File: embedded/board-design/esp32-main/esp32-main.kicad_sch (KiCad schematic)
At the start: 3 parts, among them J1 Conn_ARM_JTAG_SWD_10, U1 ESP32-WROVER-E, U2 BD48ExxG

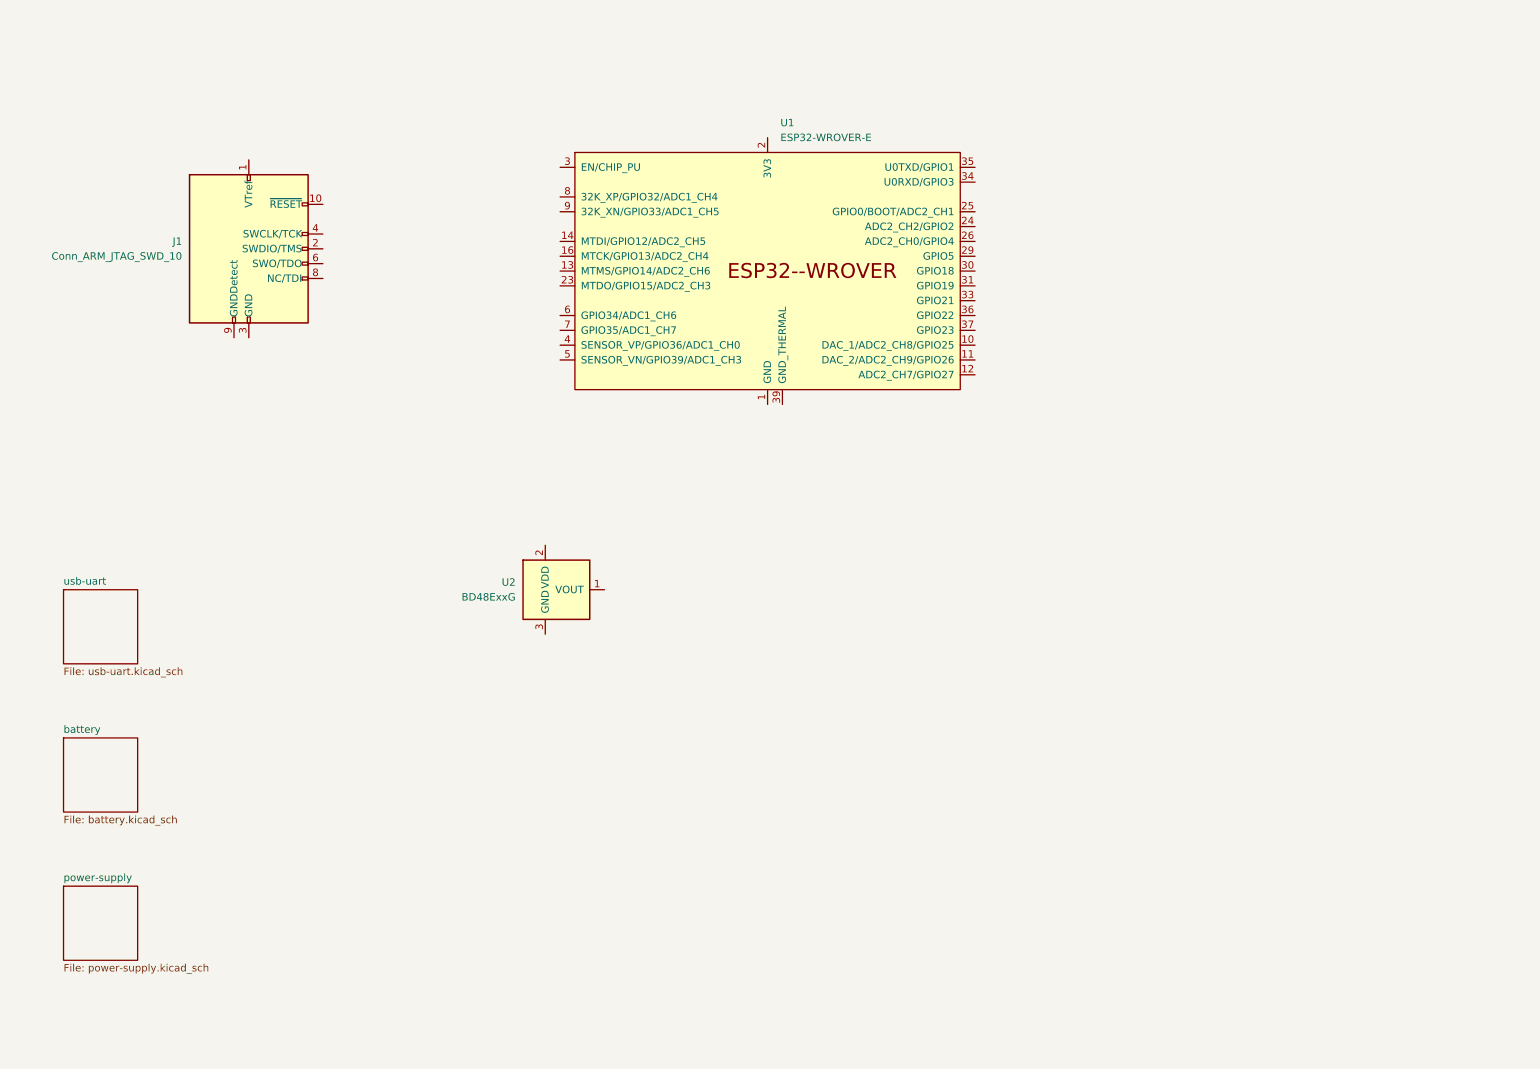
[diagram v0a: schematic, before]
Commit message: [bike-embedded-app]
Finished first schematic draft.

Signed-off-by: Nicolae-Andrei Vasile <vasilenicolaeandrei@gmail.com>
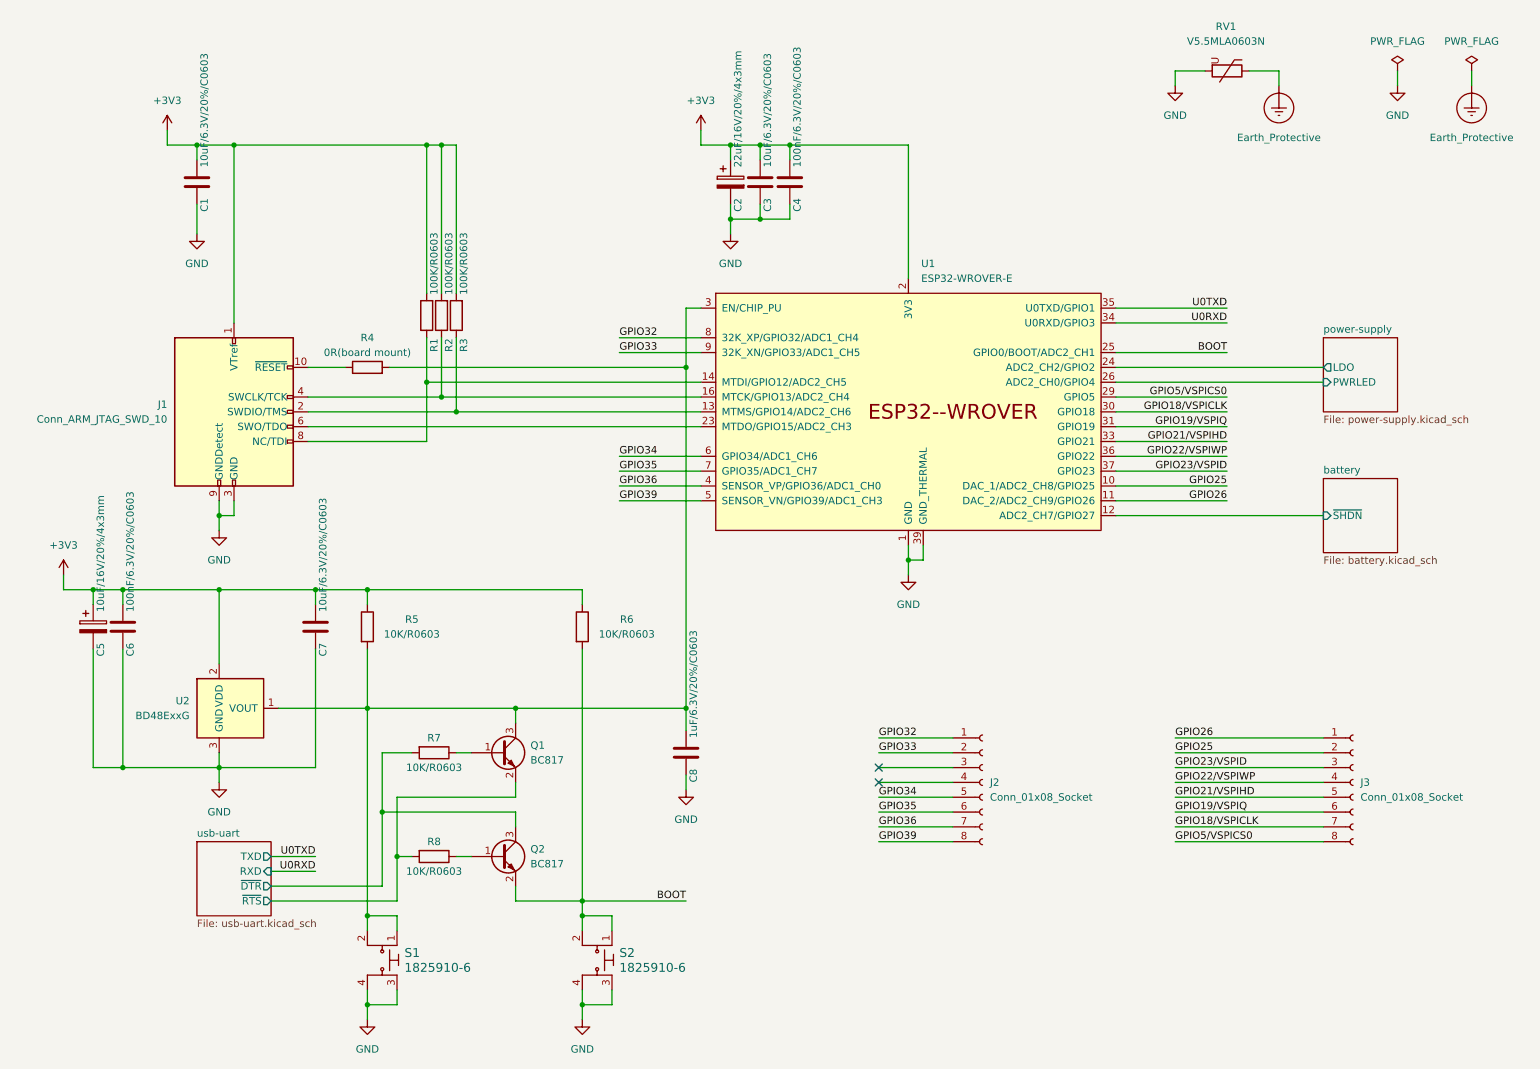
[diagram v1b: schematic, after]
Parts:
- added C1, C3, C7: 10uF/6.3V/20%/C0603, Capacitor_SMD:C_0603_1608Metric_Pad1.08x0.95mm_HandSolder, symbol Device:C
- added C2: 22uF/16V/20%/4x3mm, Capacitor_SMD:CP_Elec_4x3, symbol Device:C_Polarized
- added C4, C6: 100nF/6.3V/20%/C0603, Capacitor_SMD:C_0603_1608Metric_Pad1.08x0.95mm_HandSolder, symbol Device:C
- added C5: 10uF/16V/20%/4x3mm, Capacitor_SMD:CP_Elec_4x3, symbol Device:C_Polarized
- added C8: 1uF/6.3V/20%/C0603, Capacitor_SMD:C_0603_1608Metric_Pad1.08x0.95mm_HandSolder, symbol Device:C
- added J2, J3: Conn_01x08_Socket, Connector_Phoenix_MC:PhoenixContact_MCV_1,5_8-G-3.81_1x08_P3.81mm_Vertical, symbol Connector:Conn_01x08_Socket
- added Q1, Q2: BC817, Package_TO_SOT_SMD:SOT-23, symbol Transistor_BJT:BC817
- added R1, R2, R3: 100K/R0603, Resistor_SMD:R_0603_1608Metric_Pad0.98x0.95mm_HandSolder, symbol Device:R
- added R4: 0R(board mount), Resistor_SMD:R_0603_1608Metric_Pad0.98x0.95mm_HandSolder, symbol Device:R
- added R5, R6, R7, R8: 10K/R0603, Resistor_SMD:R_0603_1608Metric_Pad0.98x0.95mm_HandSolder, symbol Device:R
- added RV1: V5.5MLA0603N, Resistor_SMD:R_0603_1608Metric_Pad0.98x0.95mm_HandSolder, symbol Device:Varistor
- added S1, S2: 1825910-6, digikey-footprints:Switch_Tactile_THT_6x6mm, symbol dk_Tactile-Switches:1825910-6
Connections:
- net at U2.1 (VOUT): now also U1.3 (EN/CHIP_PU), C8.1, Q1.3 (C), R4.2, R5.2, S1.1, S1.2
- net +3V3: now reaches U2.2 (VDD)
- net +3V3: now also J1.1 (VTref), U1.2 (3V3), C1.1, C2.1, C3.1, C4.1, C5.1, C6.1, C7.1, R1.2, R2.2, R3.2, R5.1, R6.1
- net GND: now reaches U2.3 (GND)
- net GND: now also J1.3 (GND), J1.5 (GND), J1.9 (GNDDetect), U1.1 (GND), U1.15 (GND), U1.38 (GND), U1.39 (GND_THERMAL), C1.2, C2.2, C3.2, C4.2, C5.2, C6.2, C7.2, C8.2, RV1.2, S1.3, S1.4, S2.3, S2.4
- net GPIO25: now reaches U1.10 (DAC_1/ADC2_CH8/GPIO25)
- net GPIO25: now also J3.2 (Pin_2)
- net GPIO26: now reaches U1.11 (DAC_2/ADC2_CH9/GPIO26)
- net GPIO26: now also J3.1 (Pin_1)
- net battery/~{SHDN}: now reaches U1.12 (ADC2_CH7/GPIO27)
- net at U1.13 (MTMS/GPIO14/ADC2_CH6): now also J1.2 (SWDIO/TMS), R3.1
- net at U1.14 (MTDI/GPIO12/ADC2_CH5): now also J1.8 (NC/TDI), R1.1
- net at U1.16 (MTCK/GPIO13/ADC2_CH4): now also J1.4 (SWCLK/TCK), R2.1
- net at U1.23 (MTDO/GPIO15/ADC2_CH3): now also J1.6 (SWO/TDO)
- net power-supply/LDO: now reaches U1.24 (ADC2_CH2/GPIO2)
- net BOOT: now reaches U1.25 (GPIO0/BOOT/ADC2_CH1)
- net BOOT: now also Q2.2 (E), R6.2, S2.1, S2.2
- net power-supply/PWRLED: now reaches U1.26 (ADC2_CH0/GPIO4)
- net GPIO5/VSPICS0: now reaches U1.29 (GPIO5)
- net GPIO5/VSPICS0: now also J3.8 (Pin_8)
- net GPIO18/VSPICLK: now reaches U1.30 (GPIO18)
- net GPIO18/VSPICLK: now also J3.7 (Pin_7)
- net GPIO19/VSPIQ: now reaches U1.31 (GPIO19)
- net GPIO19/VSPIQ: now also J3.6 (Pin_6)
- net GPIO21/VSPIHD: now reaches U1.33 (GPIO21)
- net GPIO21/VSPIHD: now also J3.5 (Pin_5)
- net U0RXD: now reaches U1.34 (U0RXD/GPIO3)
- net U0TXD: now reaches U1.35 (U0TXD/GPIO1)
- net GPIO22/VSPIWP: now reaches U1.36 (GPIO22)
- net GPIO22/VSPIWP: now also J3.4 (Pin_4)
- net GPIO23/VSPID: now reaches U1.37 (GPIO23)
- net GPIO23/VSPID: now also J3.3 (Pin_3)
- net GPIO36: now reaches U1.4 (SENSOR_VP/GPIO36/ADC1_CH0)
- net GPIO36: now also J2.7 (Pin_7)
- net GPIO39: now reaches U1.5 (SENSOR_VN/GPIO39/ADC1_CH3)
- net GPIO39: now also J2.8 (Pin_8)
- net GPIO34: now reaches U1.6 (GPIO34/ADC1_CH6)
- net GPIO34: now also J2.5 (Pin_5)
- net GPIO35: now reaches U1.7 (GPIO35/ADC1_CH7)
- net GPIO35: now also J2.6 (Pin_6)
- net GPIO32: now reaches U1.8 (32K_XP/GPIO32/ADC1_CH4)
- net GPIO32: now also J2.1 (Pin_1)
- net GPIO33: now reaches U1.9 (32K_XN/GPIO33/ADC1_CH5)
- net GPIO33: now also J2.2 (Pin_2)
- net at J1.10 (~{RESET}): now also R4.1
- new net: Q2.1 (B), R8.1
- new net: Q1.1 (B), R7.1
- new net Earth_Protective: RV1.1
- new net usb-uart/~{DTR}: Q2.3 (C), R7.2
- new net usb-uart/~{RTS}: Q1.2 (E), R8.2
- no-connect marks 0 -> 2
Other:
- sheet battery ports: added ~{SHDN}; removed none
- sheet power-supply ports: added LDO, PWRLED; removed none
- sheet usb-uart ports: added RXD, TXD, ~{DTR}, ~{RTS}; removed none
- moved on the sheet: J1, U1, U2

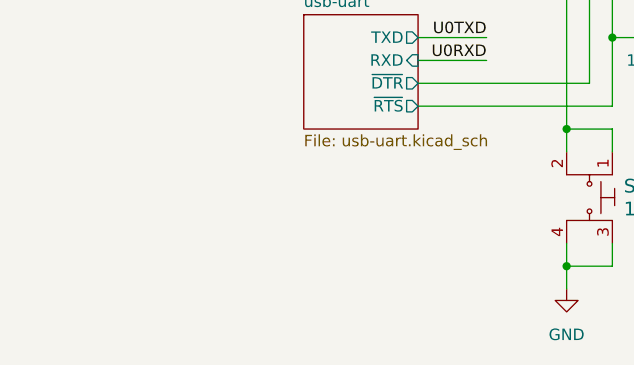
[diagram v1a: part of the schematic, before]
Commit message: [bike-embedded-app]
First draft of the part placement on PCB. No routes drawn yet. Added
entry for possible alternator.

Signed-off-by: Nicolae-Andrei Vasile <vasilenicolaeandrei@gmail.com>
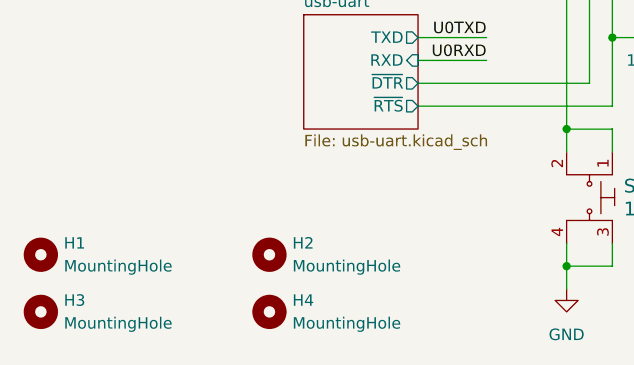
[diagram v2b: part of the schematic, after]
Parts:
- added H1, H2, H3, H4: MountingHole, MountingHole:MountingHole_2.2mm_M2, symbol Mechanical:MountingHole
- J2, J3: footprint Connector_Phoenix_MC:PhoenixContact_MCV_1,5_8-G-3.81_1x08_P3.81mm_Vertical -> Connector_Phoenix_MC:PhoenixContact_MC_1,5_8-G-3.81_1x08_P3.81mm_Horizontal

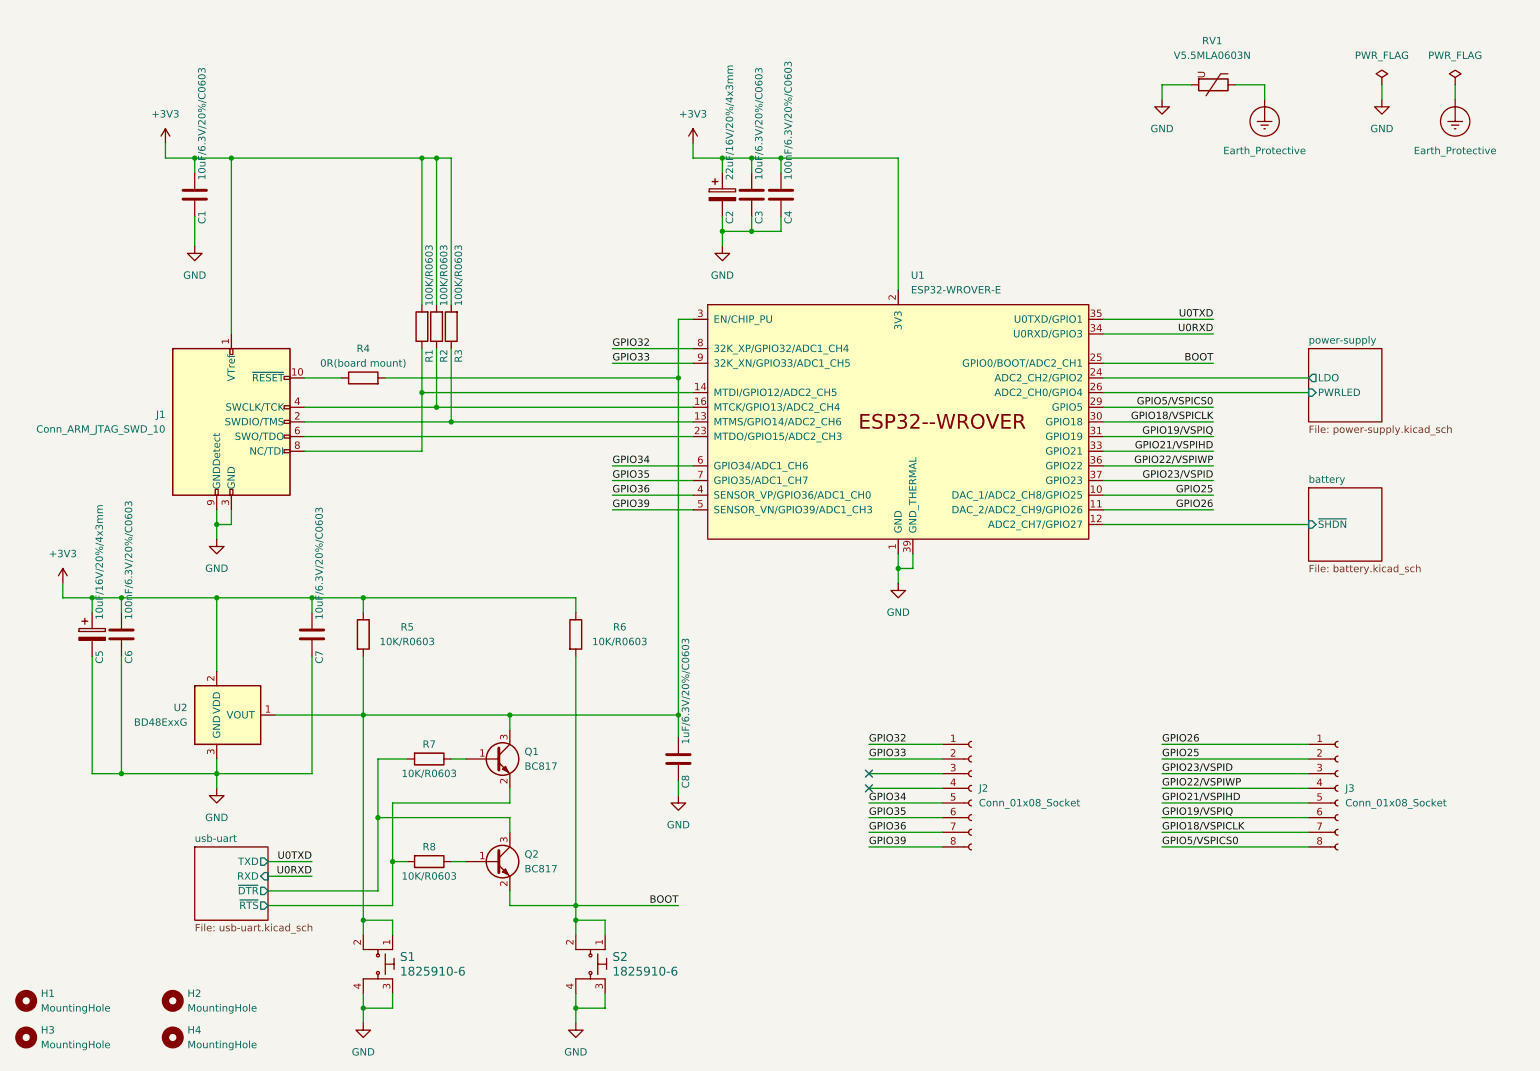
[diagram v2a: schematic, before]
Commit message: [bike-embedded-app]
Finished first draft of the embedded hardware app. PCB design
constraints follow PCBWay recommendations.

Signed-off-by: Nicolae-Andrei Vasile <vasilenicolaeandrei@gmail.com>
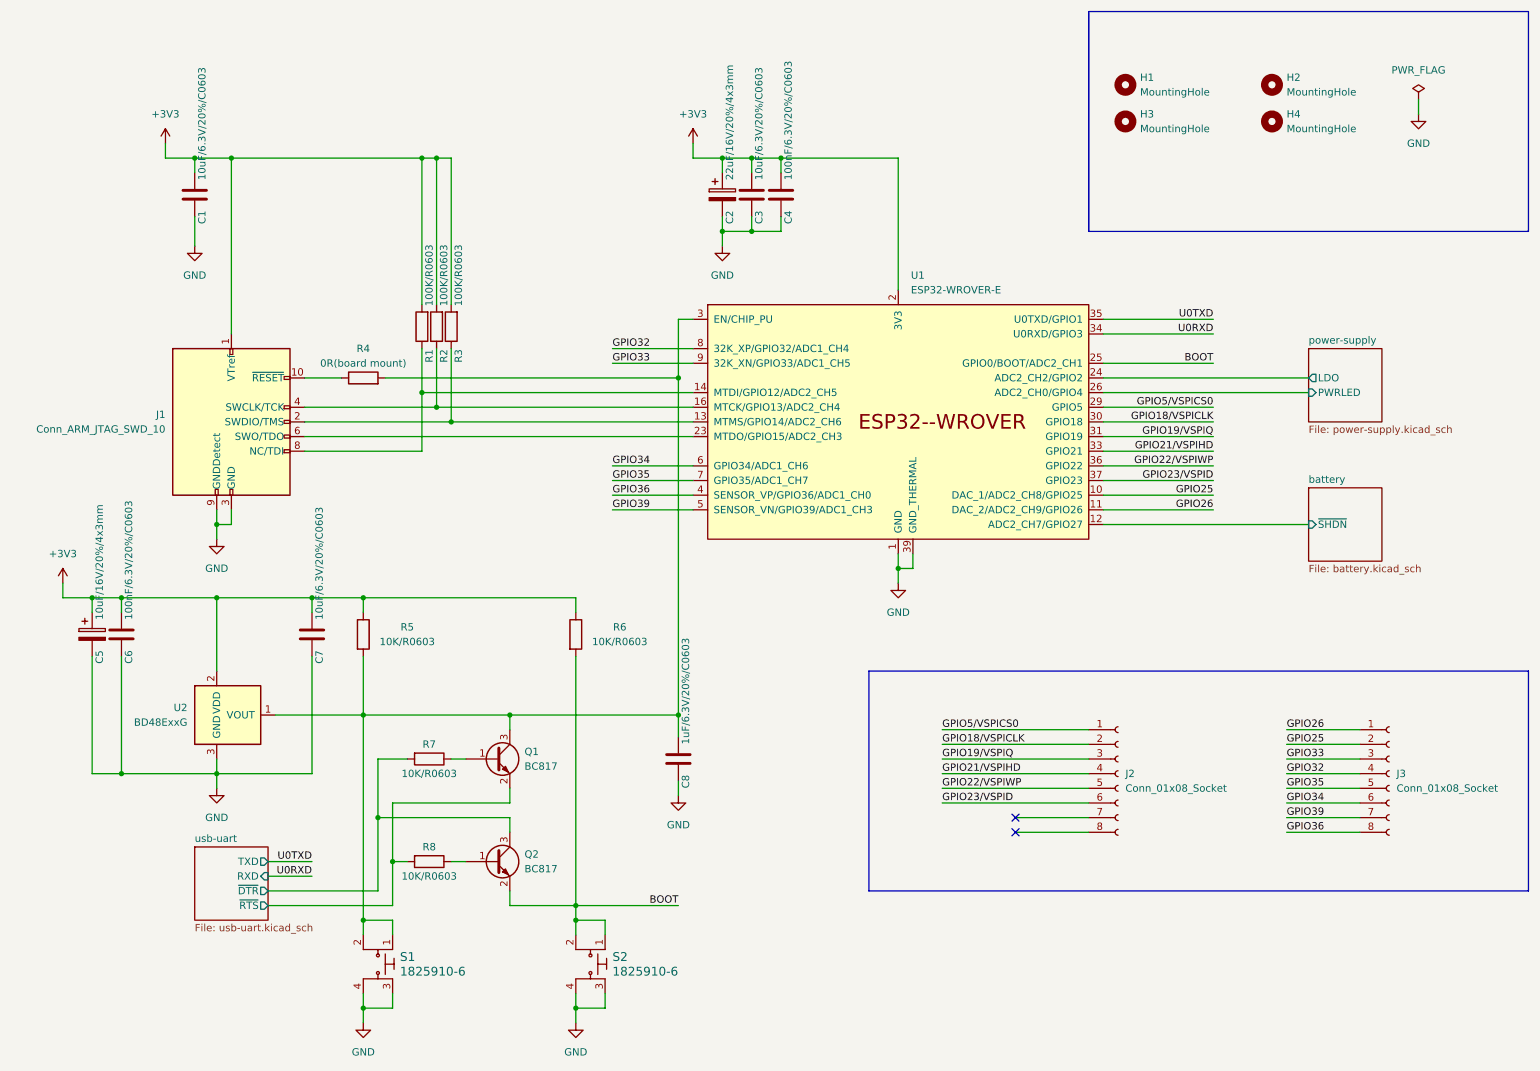
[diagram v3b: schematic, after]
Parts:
- removed RV1: V5.5MLA0603N, Resistor_SMD:R_0603_1608Metric_Pad0.98x0.95mm_HandSolder, symbol Device:Varistor
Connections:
- net GPIO18/VSPICLK: now also J2.2 (Pin_2); no longer J3.7 (Pin_7)
- net GPIO19/VSPIQ: now also J2.3 (Pin_3); no longer J3.6 (Pin_6)
- net GPIO21/VSPIHD: now also J2.4 (Pin_4); no longer J3.5 (Pin_5)
- net GPIO22/VSPIWP: now also J2.5 (Pin_5); no longer J3.4 (Pin_4)
- net GPIO23/VSPID: now also J2.6 (Pin_6); no longer J3.3 (Pin_3)
- net GPIO32: now also J3.4 (Pin_4); no longer J2.1 (Pin_1)
- net GPIO33: now also J3.3 (Pin_3); no longer J2.2 (Pin_2)
- net GPIO34: now also J3.6 (Pin_6); no longer J2.5 (Pin_5)
- net GPIO35: now also J3.5 (Pin_5); no longer J2.6 (Pin_6)
- net GPIO36: now also J3.8 (Pin_8); no longer J2.7 (Pin_7)
- net GPIO39: now also J3.7 (Pin_7); no longer J2.8 (Pin_8)
- net GPIO5/VSPICS0: now also J2.1 (Pin_1); no longer J3.8 (Pin_8)
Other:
- title: (none) -> ESP32 embedded application
- moved on the sheet: H1, H2, H3, H4, J2, J3

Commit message: [bike-embedded-app]
Signed-off-by: Nicolae-Andrei Vasile <vasilenicolaeandrei@gmail.com>
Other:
- moved on the sheet: H1, H2, H3, H4, J2, J3

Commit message: [bike-embedded-app]
Added output for 3V3. Increased mounting holes.

Signed-off-by: Nicolae-Andrei Vasile <vasilenicolaeandrei@gmail.com>
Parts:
- added D1: SMD22WS-TP, Diode_SMD:D_SOD-323_HandSoldering, symbol Device:D_Schottky
- H1, H4: footprint MountingHole:MountingHole_2.2mm_M2 -> MountingHole:MountingHole_3.2mm_M3
- H2: renamed from H3; footprint MountingHole:MountingHole_2.2mm_M2 -> MountingHole:MountingHole_3.2mm_M3
- H3: renamed from H2; footprint MountingHole:MountingHole_2.2mm_M2 -> MountingHole:MountingHole_3.2mm_M3
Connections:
- net +3V3: now also D1.2 (A)
- net GND: now also J3.2 (Pin_2)
- net GPIO18/VSPICLK: now also J2.4 (Pin_4); no longer J2.2 (Pin_2)
- net GPIO19/VSPIQ: now also J2.5 (Pin_5); no longer J2.3 (Pin_3)
- net GPIO21/VSPIHD: now also J2.6 (Pin_6); no longer J2.4 (Pin_4)
- net GPIO22/VSPIWP: now also J2.7 (Pin_7); no longer J2.5 (Pin_5)
- net GPIO23/VSPID: now also J2.8 (Pin_8); no longer J2.6 (Pin_6)
- net GPIO25: now also J3.4 (Pin_4); no longer J3.2 (Pin_2)
- net GPIO26: now also J3.3 (Pin_3); no longer J3.1 (Pin_1)
- net GPIO32: now also J3.6 (Pin_6); no longer J3.4 (Pin_4)
- net GPIO33: now also J3.5 (Pin_5); no longer J3.3 (Pin_3)
- net GPIO34: now also J3.8 (Pin_8); no longer J3.6 (Pin_6)
- net GPIO35: now also J3.7 (Pin_7); no longer J3.5 (Pin_5)
- net GPIO36: now also J2.2 (Pin_2); no longer J3.8 (Pin_8)
- net GPIO39: now also J2.1 (Pin_1); no longer J3.7 (Pin_7)
- net GPIO5/VSPICS0: now also J2.3 (Pin_3); no longer J2.1 (Pin_1)
- new net: D1.1 (K), J3.1 (Pin_1)
- no-connect marks 2 -> 0
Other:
- moved on the sheet: C1, C2, C3, C4, C5, C6, C7, C8, H1, H2, H3, H4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
